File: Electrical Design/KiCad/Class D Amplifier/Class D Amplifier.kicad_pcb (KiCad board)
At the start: 2 copper layers, 77.5 x 31.8 mm, 27 parts, among them J1 AudioJack3, J2 speakON_NL2MDXX-V, J3 Barrel_Jack, U1 TPA3136D2PWPR

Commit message: board changes
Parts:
- moved U1 0.08 mm to (144.2, 81.0)
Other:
- board text added: "QA:"
- board text removed: "QA"

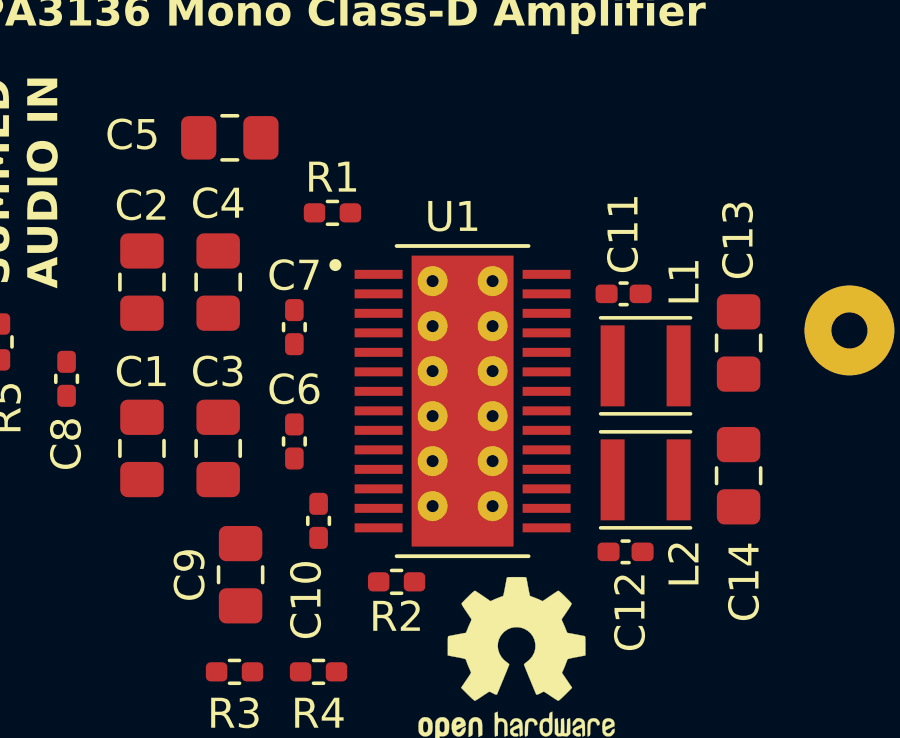
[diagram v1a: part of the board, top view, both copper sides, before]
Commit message: add PDS, modified amp footprint, organizational changes
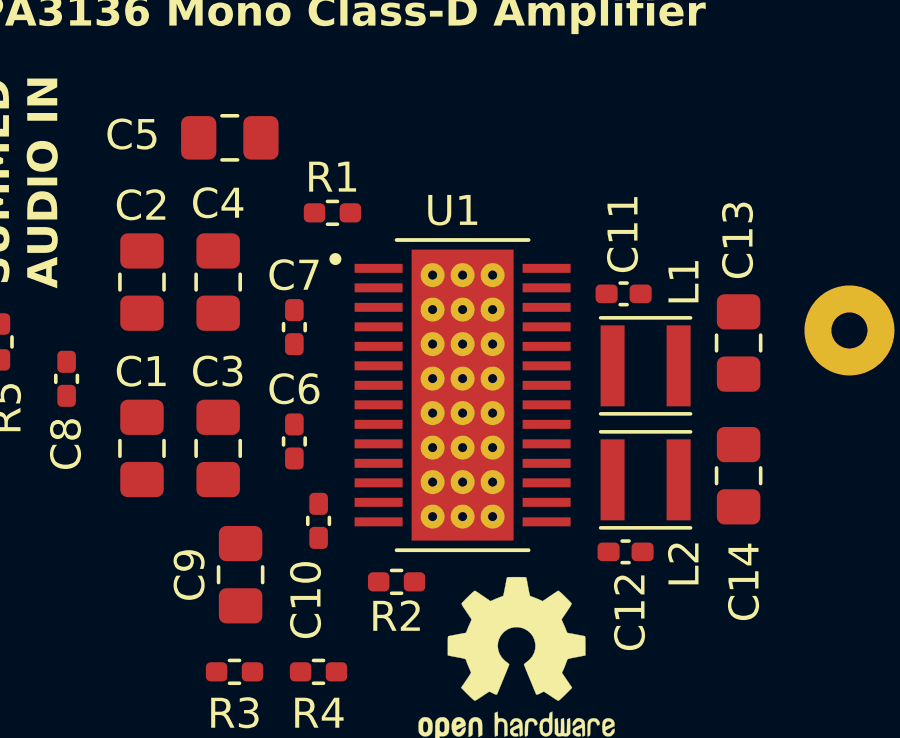
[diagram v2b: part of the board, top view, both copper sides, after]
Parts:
- moved U1 0.20 mm to (144.2, 80.8)
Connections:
- C1 pad 2: VCC -> GND
- C2 pad 1: VCC -> GND
- C3 pad 2: VCC -> GND
- C4 pad 1: VCC -> GND
- C5 pad 1: VCC -> GND
- C6 pad 2: VCC -> GND
- C7 pad 1: VCC -> GND
- C9 pad 2: Net-(U1-GVDD) -> GND
- J3 pad 1: VCC -> GND
- R1 pad 1: VCC -> GND
- R2 pad 1: VCC -> GND
- R2 pad 2: Net-(U1-PBTL) -> /SHUTDOWN
- R3 pad 2: Net-(U1-PLIMIT) -> /SHUTDOWN
- R4 pad 1: Net-(U1-PLIMIT) -> /SHUTDOWN
- R4 pad 2: Net-(U1-GVDD) -> GND
- U1 pad 10: Net-(U1-PLIMIT) -> /SHUTDOWN
- U1 pad 14: Net-(U1-PBTL) -> /SHUTDOWN
- U1 pad 15: VCC -> GND
- U1 pad 16: VCC -> GND
- U1 pad 27: VCC -> GND
- U1 pad 28: VCC -> GND
- U1 pad 7: VCC -> GND
- U1 pad 9: Net-(U1-GVDD) -> GND
